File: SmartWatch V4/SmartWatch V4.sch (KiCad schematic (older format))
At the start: 66 parts, among them J1 10118192-0001LF, J10 TestPad, J11 TestPad, J12 TestPad, J13 TestPad, J14 TestPad, J2 , J3 TestPad, J4 TestPad, J5 TestPad, J6 TestPad, J7 TestPad, J8 TestPad, J9 TestPad, Q1 FDN340P, Q2 MMBT3904, Q3 MMBT3904, Q4 FDN340P, SW1 EVQ-P7J01P, SW2 EVQ-P7J01P, U1 MAX17260, U10 TSC2003IPWR, U11 NHD-1.8-128160EF-CTXI#-T, U2 FT231XQ, U3 LP5912-3.3DRVT, U4 LP5912-2.8DRVT, U5 MCP73832-2-OT, U6 ESP32-WROOM-32, U7 NLSV4T244, U8 NLSV4T244, U9 NLSV4T244

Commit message: Changes to version 4 before sending off to production
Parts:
- J1: symbol Connector:USB_B_Micro -> CustomParts:10118192-0001LF
- U1: digikey 175-MAX17260SEWL+TCT-ND -> MAX17260SETD+-ND
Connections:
- net GND: now also J1.SH1 (SHIELD), J1.SH2 (SHIELD), J1.SH3 (SHIELD), J1.SH4 (SHIELD), J1.SH5 (SHIELD), J1.SH6 (SHIELD), U1.9 (CSPL); no longer J1.6 (Shield)
- net IO12: now also U4.4 (EN); no longer U7.2 (A1)
- net IO15: now also U7.4 (A3); no longer Q4.1 (G), R22.2
- net RXD0: now also U6.34 (RXD0/IO3); no longer U6.35 (TXD0/IO1)
- net TXD0: now also U6.35 (TXD0/IO1); no longer U6.34 (RXD0/IO3)
- net LCD_EN renamed LCD_~CS~
- net LCD_~CS~: now also U7.2 (A1); no longer U4.4 (EN)
- net LCD_~WR~ renamed LCD_LED
- net LCD_LED: now also Q4.1 (G), R22.2; no longer U7.4 (A3)
- no-connect marks 16 -> 15
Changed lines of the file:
@@
 	3100 7200 3200 7200
-$Comp
-L Connector:USB_B_Micro J1
-U 1 1 5E6DBEE6
-P 800 5900
-F 0 "J1" H 700 6400 50  0000 C CNN
-F 1 "10118192-0001LF" H 1000 6300 50  0000 C CNN
-F 2 "CustomFootprints:AMPHENOL_10118192-0001LF" H 800 5900 50  0001 L BNN
-F 3 "Amphenol ICC" H 800 5900 50  0001 L BNN
-F 4 "None" H 800 5900 50  0001 L BNN "Field4"
-F 5 "Single Port 5 Contact Horizontal Right Angle Shielded Micro B USB 2.0 Connector" H 800 5900 50  0001 L BNN "Field5"
-F 6 "609-4613-1-ND" H 800 5900 50  0001 L BNN "digikey"
-F 7 "10118192-0001LF" H 800 5900 50  0001 L BNN "Field7"
-F 8 "https://www.digikey.com/product-detail/en/amphenol-icc-fci/10118192-0001LF/609-4613-1-ND/2785378?utm_source=snapeda&utm_medium=aggregator&utm_campaign=symbol" H 800 5900 50  0001 L BNN "Field8"
-	1    800  5900
-	1    0    0    -1
-$EndComp
 $Comp
 L Device:R R2
@@
 	0    -1   -1   0
 $EndComp
-Text Label 1400 5700 2    50   ~ 0
+Text Label 1400 5800 2    50   ~ 0
 VBUS
 Wire Wire Line
-	1100 5700 1400 5700
+	1100 5800 1400 5800
 Wire Wire Line
 	1900 5900 2400 5900
@@
 Text Label 5750 5200 2    50   ~ 0
 RXD0
+Text Label 7300 1850 2    50   ~ 0
+RXD0
 Text Label 7300 1650 2    50   ~ 0
-RXD0
-Text Label 7300 1850 2    50   ~ 0
 TXD0
-Wire Bus Line
-	550  7600 550  4700
 Text Notes 550  7550 0    50   ~ 0
 CBUS0 needs to be configured to TX&RXLED# using the FT_PROG utility\n
@@
 Text Label 7100 2150 2    50   ~ 0
 IO12
-Wire Wire Line
-	1300 6000 1400 5900
-Wire Wire Line
-	1400 5900 1600 5900
-Wire Wire Line
-	1100 6000 1300 6000
-Wire Wire Line
-	1600 6000 1400 6000
-Wire Wire Line
-	1400 6000 1300 5900
-Wire Wire Line
-	1300 5900 1100 5900
 NoConn ~ 1100 6100
-Wire Wire Line
-	700  6300 700  6400
-Wire Wire Line
-	700  6400 750  6400
-Wire Wire Line
-	800  6400 800  6300
-Wire Wire Line
-	750  6400 750  6450
-Connection ~ 750  6400
-Wire Wire Line
-	750  6400 800  6400
 $Comp
 L power:GND #PWR0108
 U 1 1 5E7C1DBF
-P 750 6450
-F 0 "#PWR0108" H 750 6200 50  0001 C CNN
-F 1 "GND" H 755 6277 50  0000 C CNN
-F 2 "" H 750 6450 50  0001 C CNN
-F 3 "" H 750 6450 50  0001 C CNN
-	1    750  6450
+P 1250 6450
+F 0 "#PWR0108" H 1250 6200 50  0001 C CNN
+F 1 "GND" H 1255 6277 50  0000 C CNN
+F 2 "" H 1250 6450 50  0001 C CNN
+F 3 "" H 1250 6450 50  0001 C CNN
+	1    1250 6450
 	1    0    0    -1
 $EndComp
@@
 Wire Wire Line
 	6900 2850 7450 2850
-Text Label 7450 2150 2    50   ~ 0
+Text Label 7450 2050 2    50   ~ 0
 LCD_~CS~
 Text Label 7450 2250 2    50   ~ 0
@@
 Wire Bus Line
 	550  550  550  4650
-Text Label 7450 2450 2    50   ~ 0
+Text Label 7450 2550 2    50   ~ 0
 LCD_LED
 Wire Wire Line
@@
 Wire Wire Line
 	6900 2050 7450 2050
-Text Label 7450 2050 2    50   ~ 0
+Text Label 7450 2150 2    50   ~ 0
 LCD_EN
 Text Label 2950 2650 0    50   ~ 0
@@
 Wire Wire Line
 	6900 2650 7450 2650
-Text Label 7450 2550 2    50   ~ 0
+Text Label 7450 2450 2    50   ~ 0
 LCD_~WR~
 Text Label 7450 2650 2    50   ~ 0
@@
 F 2 "CustomFootprints:TDFN16-EP" H 1150 4950 50  0001 C CNN
 F 3 "https://datasheets.maximintegrated.com/en/ds/MAX17260.pdf" H 1150 4950 50  0001 C CNN
-F 4 "175-MAX17260SEWL+TCT-ND" H 850 4850 50  0001 C CNN "digikey"
+F 4 "MAX17260SETD+-ND" H 850 4850 50  0001 C CNN "digikey"
 	1    1800 3800
 	1    0    0    -1
@@
 	1    0    0    -1
 $EndComp
-NoConn ~ 1400 3950
 Text Notes 550  7750 0    50   ~ 0
 Lithium Ion Battery: https://www.digikey.com/product-detail/en/jauch-quartz/LP333437JU-PCM-WIRES-50MM/1908-1390-ND/9562753 (Not final)\n
+$Comp
+L power:GND #PWR0142
+U 1 1 5EB73B93
+P 1400 3950
+F 0 "#PWR0142" H 1400 3700 50  0001 C CNN
+F 1 "GND" H 1405 3777 50  0000 C CNN
+F 2 "" H 1400 3950 50  0001 C CNN
+F 3 "" H 1400 3950 50  0001 C CNN
+	1    1400 3950
+	1    0    0    -1
+$EndComp
+$Comp
+L CustomParts:10118192-0001LF J1
+U 1 1 5E6DBEE6
+P 800 6100
+F 0 "J1" H 650 6700 50  0000 C CNN
+F 1 "10118192-0001LF" H 650 6550 50  0000 C CNN
+F 2 "CustomFootprints:AMPHENOL_10118192-0001LF" H 800 6100 50  0001 L BNN
+F 3 "Amphenol ICC" H 800 6100 50  0001 L BNN
+F 4 "None" H 800 6100 50  0001 L BNN "Field4"
+F 5 "Single Port 5 Contact Horizontal Right Angle Shielded Micro B USB 2.0 Connector" H 800 6100 50  0001 L BNN "Field5"
+F 6 "609-4613-1-ND" H 800 6100 50  0001 L BNN "digikey"
+F 7 "10118192-0001LF" H 800 6100 50  0001 L BNN "Field7"
+F 8 "https://www.digikey.com/product-detail/en/amphenol-icc-fci/10118192-0001LF/609-4613-1-ND/2785378?utm_source=snapeda&utm_medium=aggregator&utm_campaign=symbol" H 800 6100 50  0001 L BNN "Field8"
+	1    800  6100
+	-1   0    0    -1
+$EndComp
+Wire Wire Line
+	1600 5900 1100 5900
+Wire Wire Line
+	1100 6000 1600 6000
+Wire Wire Line
+	1100 6400 1250 6400
+Wire Wire Line
+	1250 6400 1250 6450
+Wire Wire Line
+	1100 6200 1250 6200
+Wire Wire Line
+	1250 6200 1250 6400
+Connection ~ 1250 6400
+Wire Bus Line
+	550  4700 550  7600
 $EndSCHEMATC

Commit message: Edits to Rev 4 board
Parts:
- removed Q4: FDN340P, Package_TO_SOT_SMD:SOT-23, symbol Device:Q_PMOS_GSD
- removed R22: 100k, Resistor_SMD:R_0603_1608Metric, symbol Device:R
- removed U11: NHD-1.8-128160EF-CTXI#-T, CustomFootprints:LCD_NHD-1.8-128160EF-CTXI#-T, symbol CustomParts:NHD-1.8-128160EF-CTXI#-T
- removed U7, U8, U9: NLSV4T244, CustomFootprints:NLSV4T244MUTAG, symbol CustomParts:NLSV4T244
- added A1: ZJY117, CustomFootprints:ZJY117, symbol CustomParts:ZJY117
- added J15, J16, J17, J18, J19, J20: TestPad, CustomFootprints:TESTPAD, symbol CustomParts:TestPad
- added Q4: 2N7002K, Package_TO_SOT_SMD:SOT-23, symbol Device:Q_NMOS_GSD
- R20: value 100k -> 0 (NC); digikey CR0603-JW-104ELFCT-ND -> 311-0.0GRCT-ND
- U4: value LP5912-2.8DRVT -> LP5912-3.3DRVT; digikey 296-44237-1-ND -> 296-44153-1-ND
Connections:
- net LCD_DB3 is gone; now on net I2C_SDA: U6.9 (IO33)
- net LCD_DB4 is gone; now on net I2C_SCL: U6.8 (IO32)
- net +3V3: no longer R4.2
- net BAT+: now also R4.2
- net GND: now also R20.1, A1.13 (GND), A1.2 (GND), A1.5 (GND), Q4.2 (S)
- net I2C_SCL: no longer U6.36 (IO22)
- net I2C_SDA: no longer U6.37 (IO23)
- net IO12: no longer U4.4 (EN)
- net LCD_LED: now also Q4.1 (G)
- net X+: now also A1.16 (XL)
- net X-: now also A1.18 (XR)
- net Y+: now also A1.15 (YU)
- net Y-: now also A1.17 (YD)
- net +2V8 renamed LCD_PWR
- net LCD_PWR: now also A1.10 (VCC), A1.11 (IOVCC), A1.4 (LED+); no longer R20.1
- net LCD_DB0: no longer names the net of U6.12 (IO27)
- net LCD_DB0: now also J20.1
- net LCD_DB1: no longer names the net of U6.11 (IO26)
- net LCD_DB1: now also J19.1
- net LCD_DB2: no longer names the net of U6.10 (IO25)
- net LCD_DB2: now also J18.1
- net LCD_DB5 renamed LCD_CS
- net LCD_CS: now also A1.12 (CS)
- net LCD_DB6 renamed LCD_A0
- net LCD_A0: now also A1.7 (A0)
- net LCD_DB7: no longer names the net of U6.31 (IO19)
- net LCD_DB7: now also J17.1
- net LCD_~CS~: no longer names the net of U6.29 (IO5)
- net LCD_~CS~: now also J15.1
- net LCD_~DC~ renamed LCD_SCK
- net LCD_SCK: now also A1.9 (SCK)
- net LCD_~RD~: no longer names the net of U6.28 (IO17)
- net LCD_~RD~: now also J16.1
- net LCD_~RST~ renamed LCD_CATHODE
- net LCD_CATHODE: now also A1.3 (LED-), Q4.3 (D); no longer U6.16 (IO13)
- new net LCD_EN: U4.4 (EN), U6.16 (IO13)
- new net LCD_MOSI: A1.8 (SDA), U6.37 (IO23)
- new net LCD_RST: A1.6 (RES), U6.36 (IO22)
- no-connect marks 15 -> 17
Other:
- note removed: "TODO: \n- double check power management circuitry\n- go over checklist from last revision"
- moved on the sheet: U6

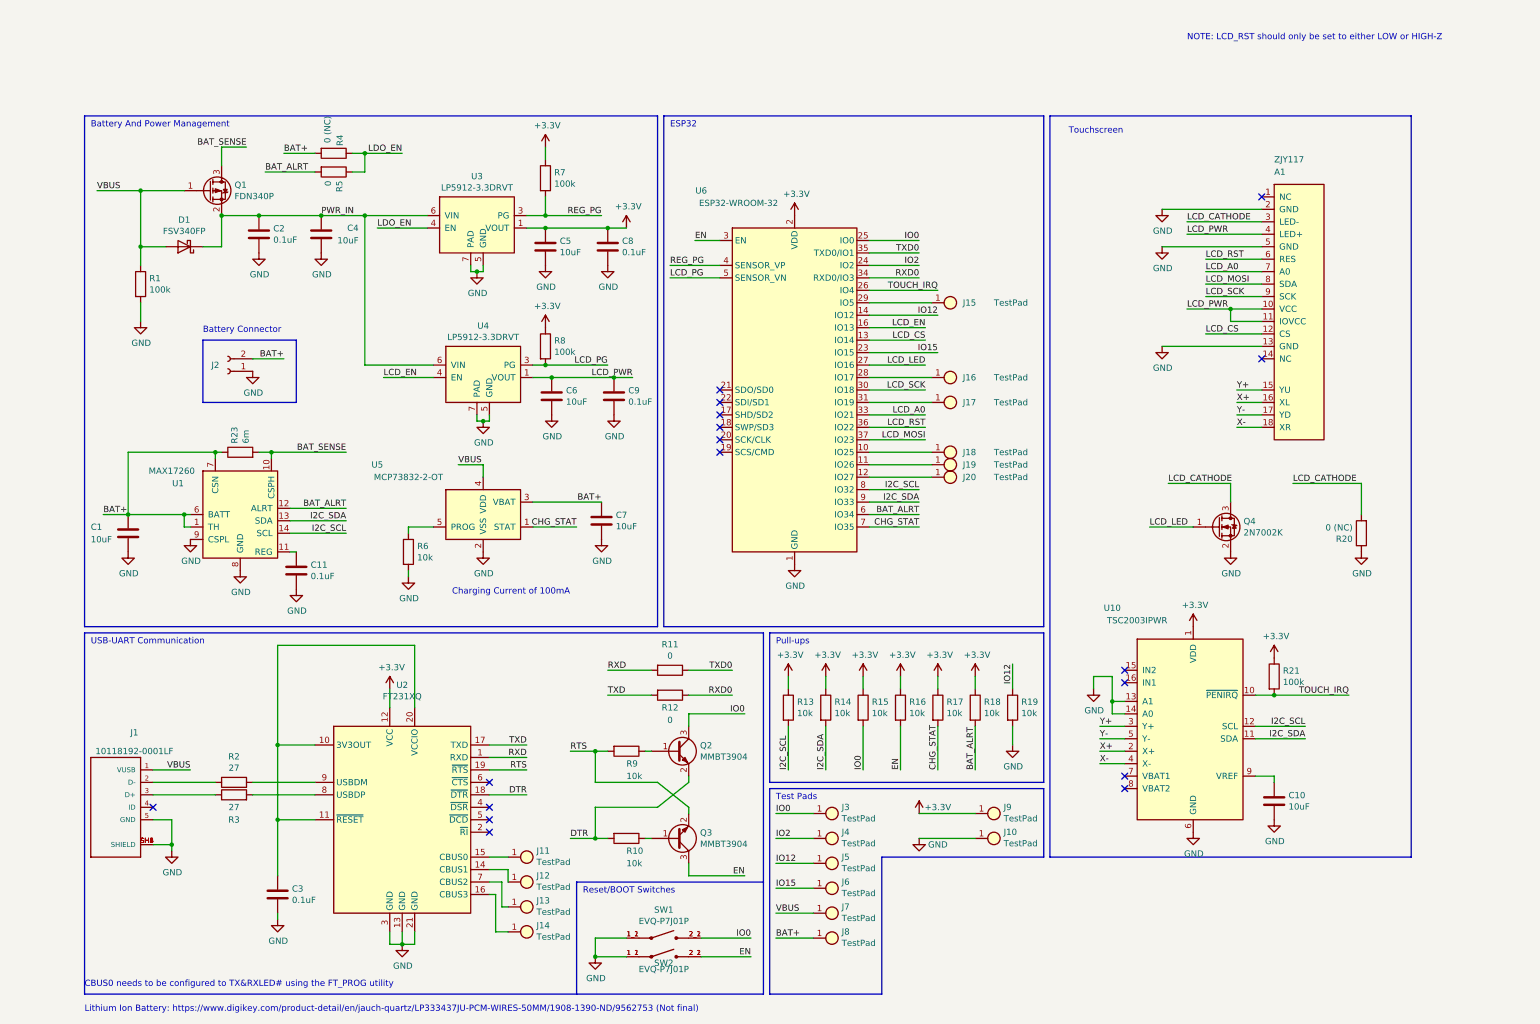
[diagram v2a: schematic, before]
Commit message: Finished design of Rev 4.1 board and ordered
- Also created an I2C device test program to aid assembly and future code
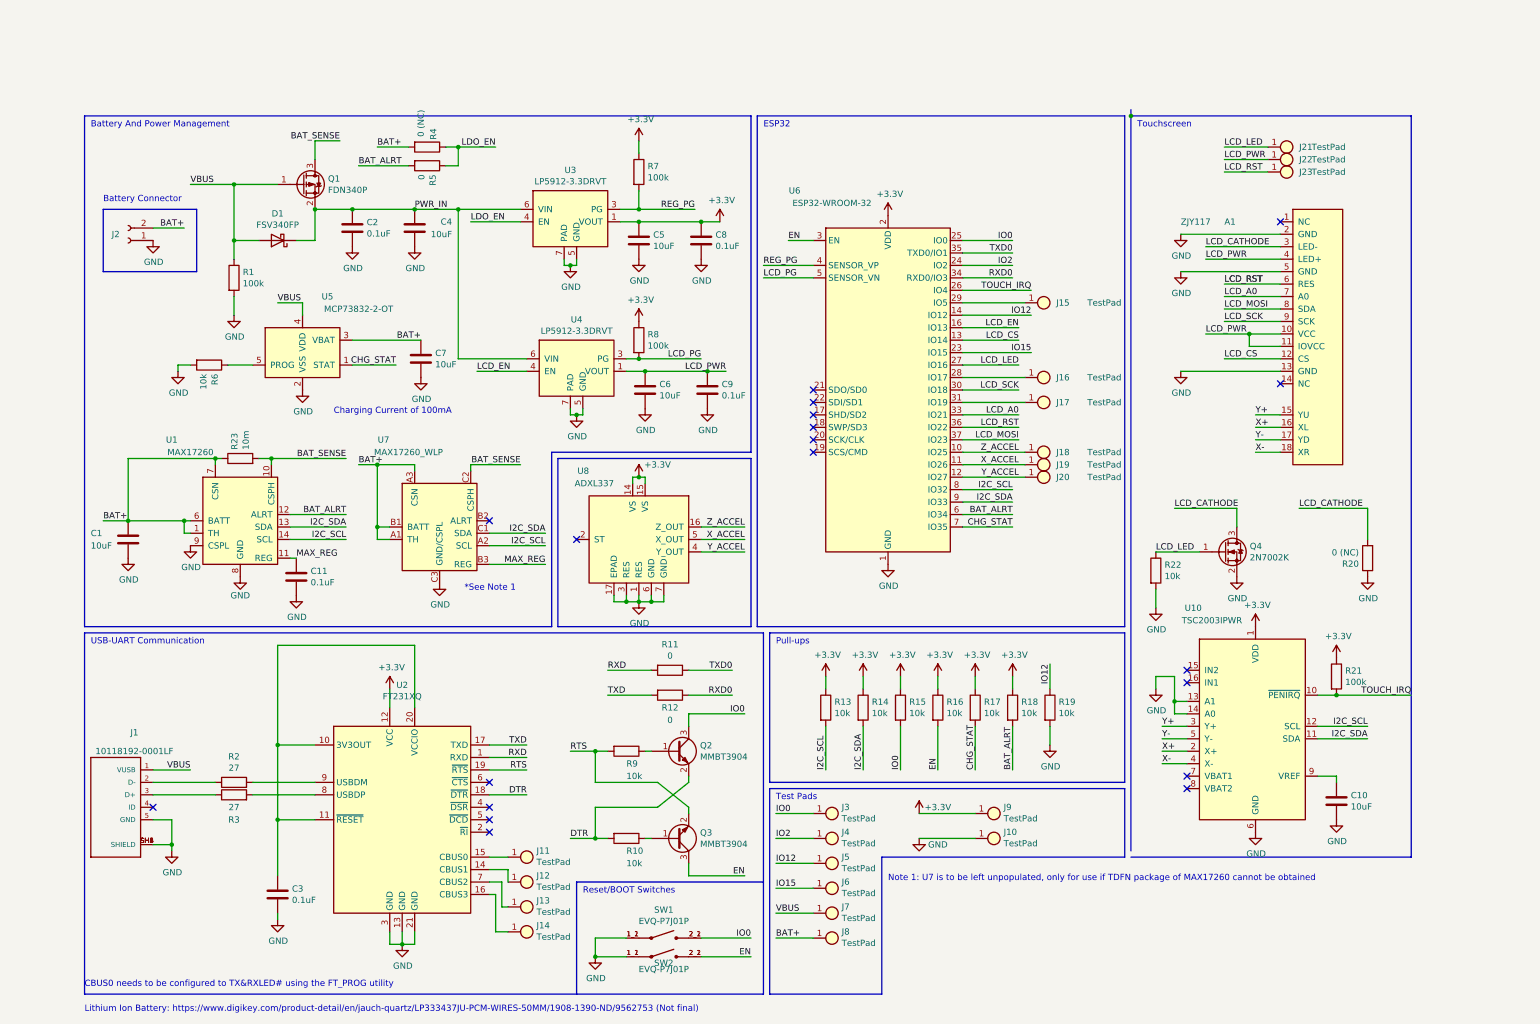
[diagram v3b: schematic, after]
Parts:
- added J21, J22, J23: TestPad, CustomFootprints:TESTPAD, symbol CustomParts:TestPad
- added R22: 10k, Resistor_SMD:R_0603_1608Metric, symbol Device:R
- added U7: MAX17260_WLP, CustomFootprints:Maxim_WLP-9_1.595x1.415_Layout3x3_P0.4mm_Ball0.27mm_Pad0.25mm_NSMD, symbol CustomParts:MAX17260_WLP
- added U8: ADXL337, CustomFootprints:ADXL337BCPZ-RL, symbol CustomParts:ADXL337
- R23: value 6m -> 10m; digikey RHM.006AKCT-ND -> RL12T.010JCT-ND
- U1: digikey MAX17260SETD+-ND -> 175-MAX17260SEWL+TCT-ND
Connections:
- net +3V3: now also U8.14 (VS), U8.15 (VS)
- net BAT+: now also U7.A1 (TH), U7.A3 (CSN), U7.B1 (BATT)
- net BAT_SENSE: now also U7.C2 (CSPH)
- net GND: now also R22.2, U7.C3 (GND/CSPL), U8.1 (RES), U8.17 (EPAD), U8.3 (RES), U8.6 (GND), U8.7 (GND)
- net I2C_SCL: now also U7.A2 (SCL)
- net I2C_SDA: now also U7.C1 (SDA)
- net LCD_LED: now also J21.1, R22.1
- net LCD_PWR: now also J22.1
- net LCD_RST: now also J23.1
- net Z_ACCEL: now reaches J18.1, U6.10 (IO25)
- net Z_ACCEL: now also U8.16 (Z_OUT)
- net X_ACCEL: now reaches J19.1, U6.11 (IO26)
- net X_ACCEL: now also U8.5 (X_OUT)
- net Y_ACCEL: now reaches J20.1, U6.12 (IO27)
- net Y_ACCEL: now also U8.4 (Y_OUT)
- net MAX_REG: now reaches C11.1, U1.11 (REG)
- net MAX_REG: now also U7.B3 (REG)
- no-connect marks 17 -> 19
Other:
- note added: "*See Note 1\n\n"
- note added: "Note 1: U7 is to be left unpopulated, only for use if TDFN package of MAX17260 cannot be obtained"
- note removed: "NOTE: LCD_RST should only be set to either LOW or HIGH-Z\n"
- moved on the sheet: A1, C1, C10, C11, C2, C4, C5, C6, C7, C8, C9, D1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

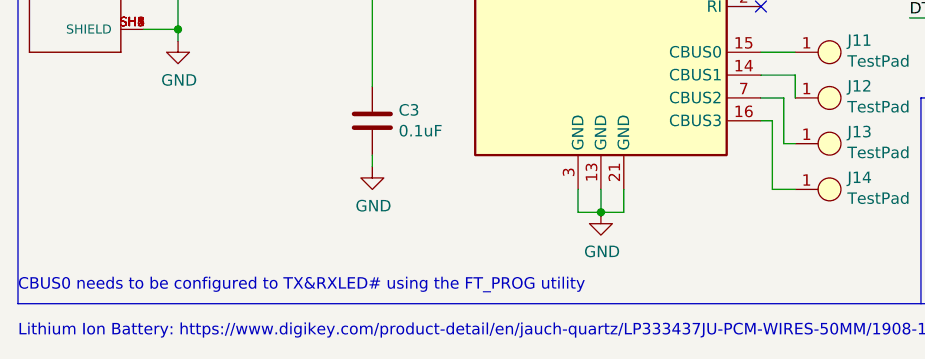
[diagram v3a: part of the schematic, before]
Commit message: Started work on software for the project. Basic communication with I2C devices and driving the touch screen
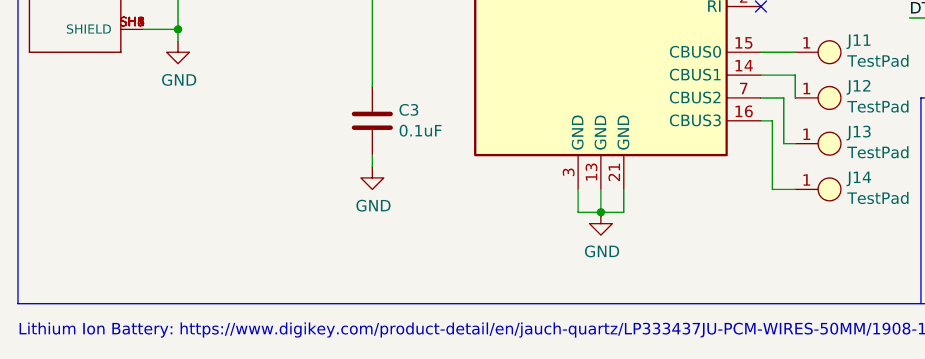
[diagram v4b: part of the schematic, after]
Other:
- note removed: "CBUS0 needs to be configured to TX&RXLED# using the FT_PROG utility\n"
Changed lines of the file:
@@
 Text Label 8000 1650 2    50   ~ 0
 TXD0
-Text Notes 550  7550 0    50   ~ 0
-CBUS0 needs to be configured to TX&RXLED# using the FT_PROG utility\n
 Wire Wire Line
 	7600 1550 8000 1550
